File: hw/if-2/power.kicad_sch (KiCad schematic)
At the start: 21 parts, among them J5 Conn_01x02, U10 NCP1117-5.0_SOT223, U11 NCP1117-3.3_SOT223

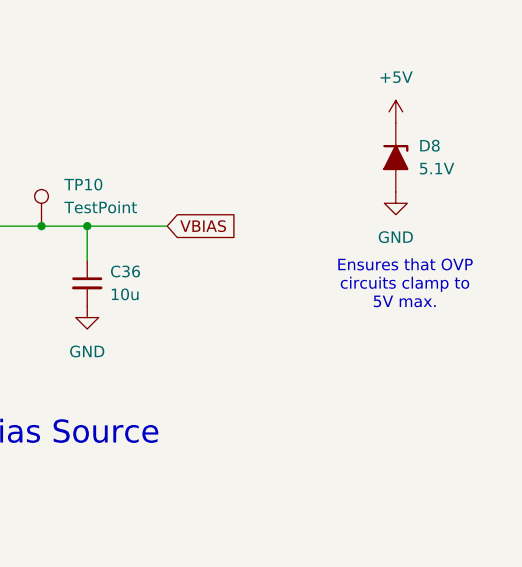
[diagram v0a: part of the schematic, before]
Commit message: Documentation improvements, moved a OVP circuit
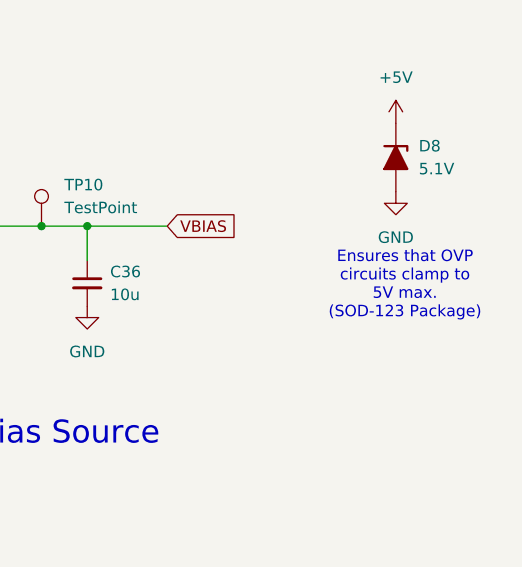
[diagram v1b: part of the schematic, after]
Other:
- note added: "Ensures that OVP circuits clamp to 5V max. (SOD-123 Package)"
- note removed: "Ensures that OVP circuits clamp to 5V max."
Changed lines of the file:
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@@
 	(title_block
 		(title "COS/CTCSS/PTT Controls (Radio 1)")
-		(date "2025-05-13")
+		(date "2025-05-31")
 		(rev "2")
 		(company "Bruce MacKinnon KC1FSZ")
@@
 		)
 	)
-	(text "Ensures that OVP \ncircuits clamp to \n5V max."
+	(text "Ensures that OVP \ncircuits clamp to \n5V max.\n(SOD-123 Package)"
 		(exclude_from_sim no)
 		(at 248.666 56.134 0)

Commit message: Updated audio file to 16K
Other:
- note added: "Band is on the cathode (this end)"
- note added: "Ensures that all OVP circuits clamp to 5V max. (SOD-123 Package)"
- note added: "Reverse polarity protection (marking "KL")"
- note removed: "Ensures that OVP circuits clamp to 5V max. (SOD-123 Package)"
- note removed: "Reverse polarity protection"
- title: COS/CTCSS/PTT Controls (Radio 1) -> Power
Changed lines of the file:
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@@
 	(paper "USLetter")
 	(title_block
-		(title "COS/CTCSS/PTT Controls (Radio 1)")
+		(title "Power")
 		(date "2025-06-21")
 		(rev "3")
@@
 		(comment 1 "Copyright (C) Bruce MacKinnon, 2025")
 		(comment 2 "NOT FOR COMMERCIAL USE")
+	)
+	(text "Band is on the \ncathode (this end)"
+		(exclude_from_sim no)
+		(at 237.744 37.846 0)
+		(effects
+			(font
+				(size 1.27 1.27)
+			)
+		)
 	)
 	(text "TVS Diode (12V_{wm}) for protection\nagainst ESD and other over-voltage transients."
@@
 		)
 	)
-	(text "Ensures that OVP \ncircuits clamp to \n5V max.\n(SOD-123 Package)"
+	(text "Ensures that all OVP \ncircuits clamp to \n5V max.\n(SOD-123 Package)"
 		(exclude_from_sim no)
 		(at 248.666 56.134 0)
@@
 		)
 	)
-	(text "Reverse polarity protection"
+	(text "Reverse polarity protection (marking \"KL\")"
 		(exclude_from_sim no)
 		(at 142.494 79.756 0)

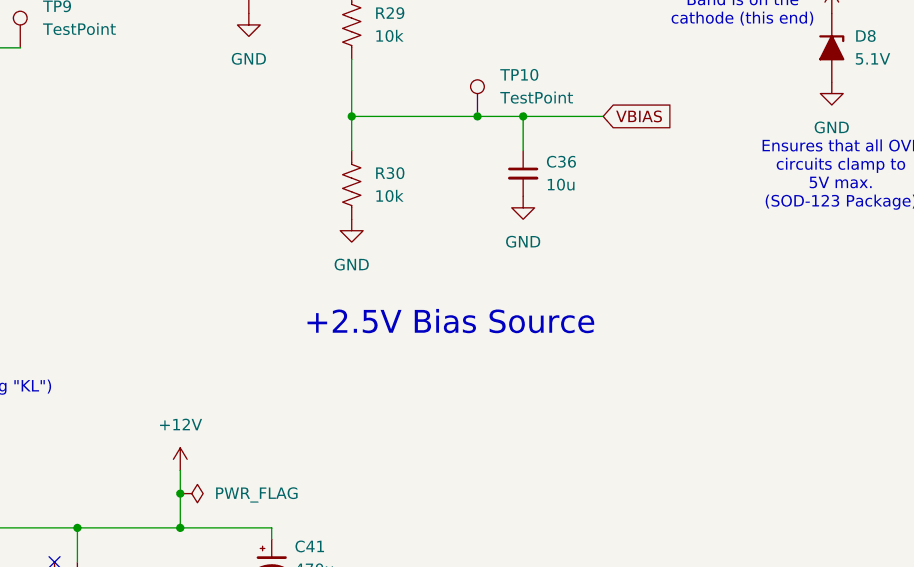
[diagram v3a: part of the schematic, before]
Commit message: Updating schematics, create new mini-board for radio interface
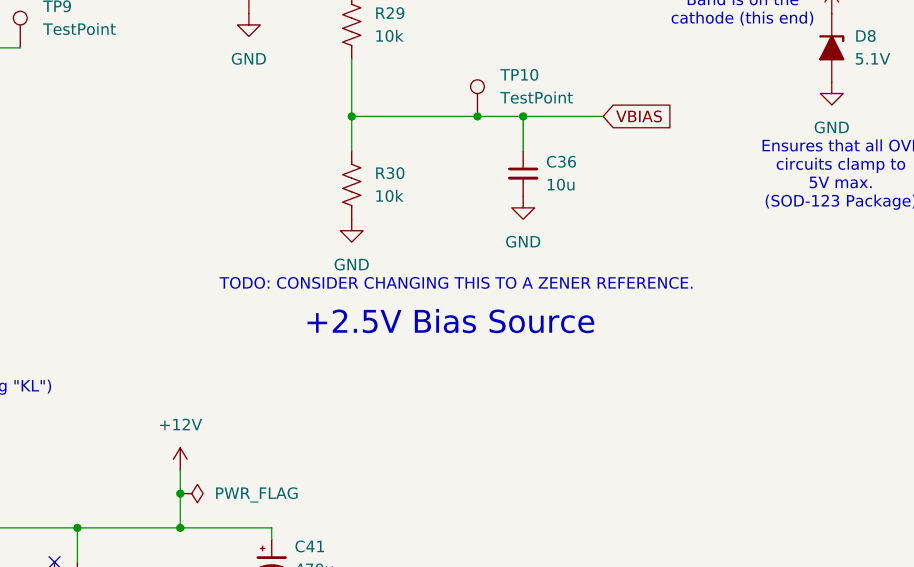
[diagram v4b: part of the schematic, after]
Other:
- note added: "TODO: CONSIDER CHANGING THIS TO A ZENER REFERENCE."
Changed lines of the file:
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@@
+		)
+	)
+	(text "TODO: CONSIDER CHANGING THIS TO A ZENER REFERENCE."
+		(exclude_from_sim no)
+		(at 205.994 68.326 0)
+		(effects
+			(font
+				(size 1.27 1.27)
+				(color 255 2 2 1)
+			)
 		)
 	)

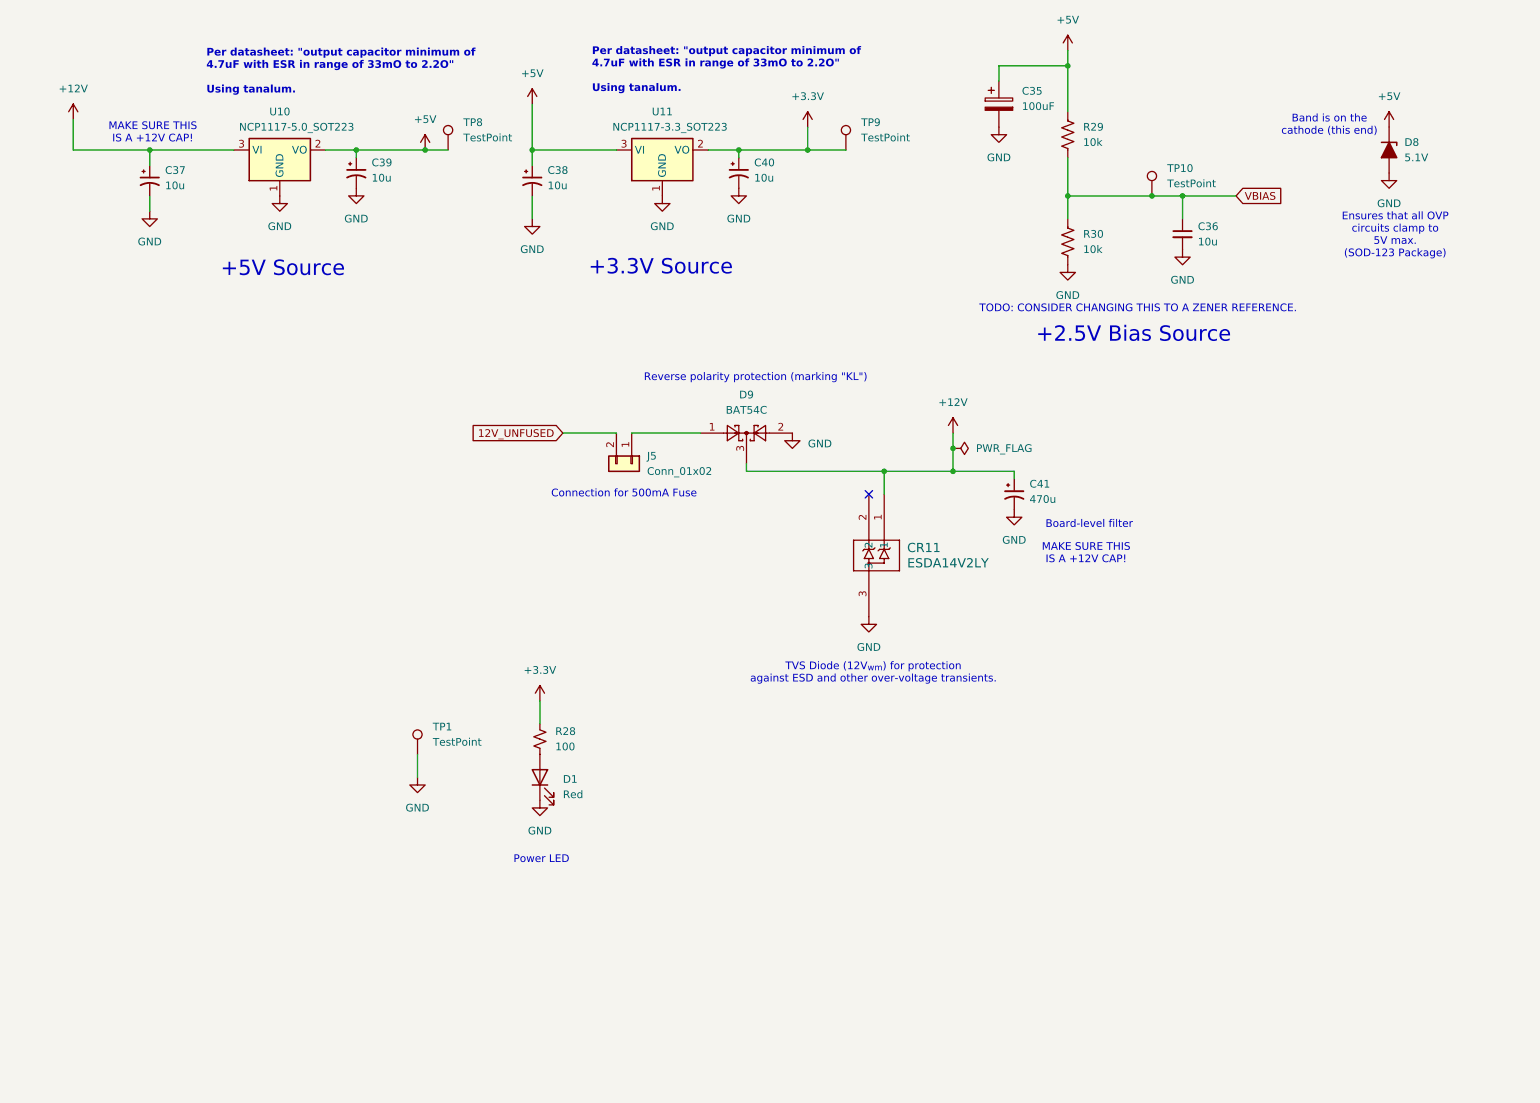
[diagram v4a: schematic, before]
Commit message: Updating schematics, create new mini-board for radio interface
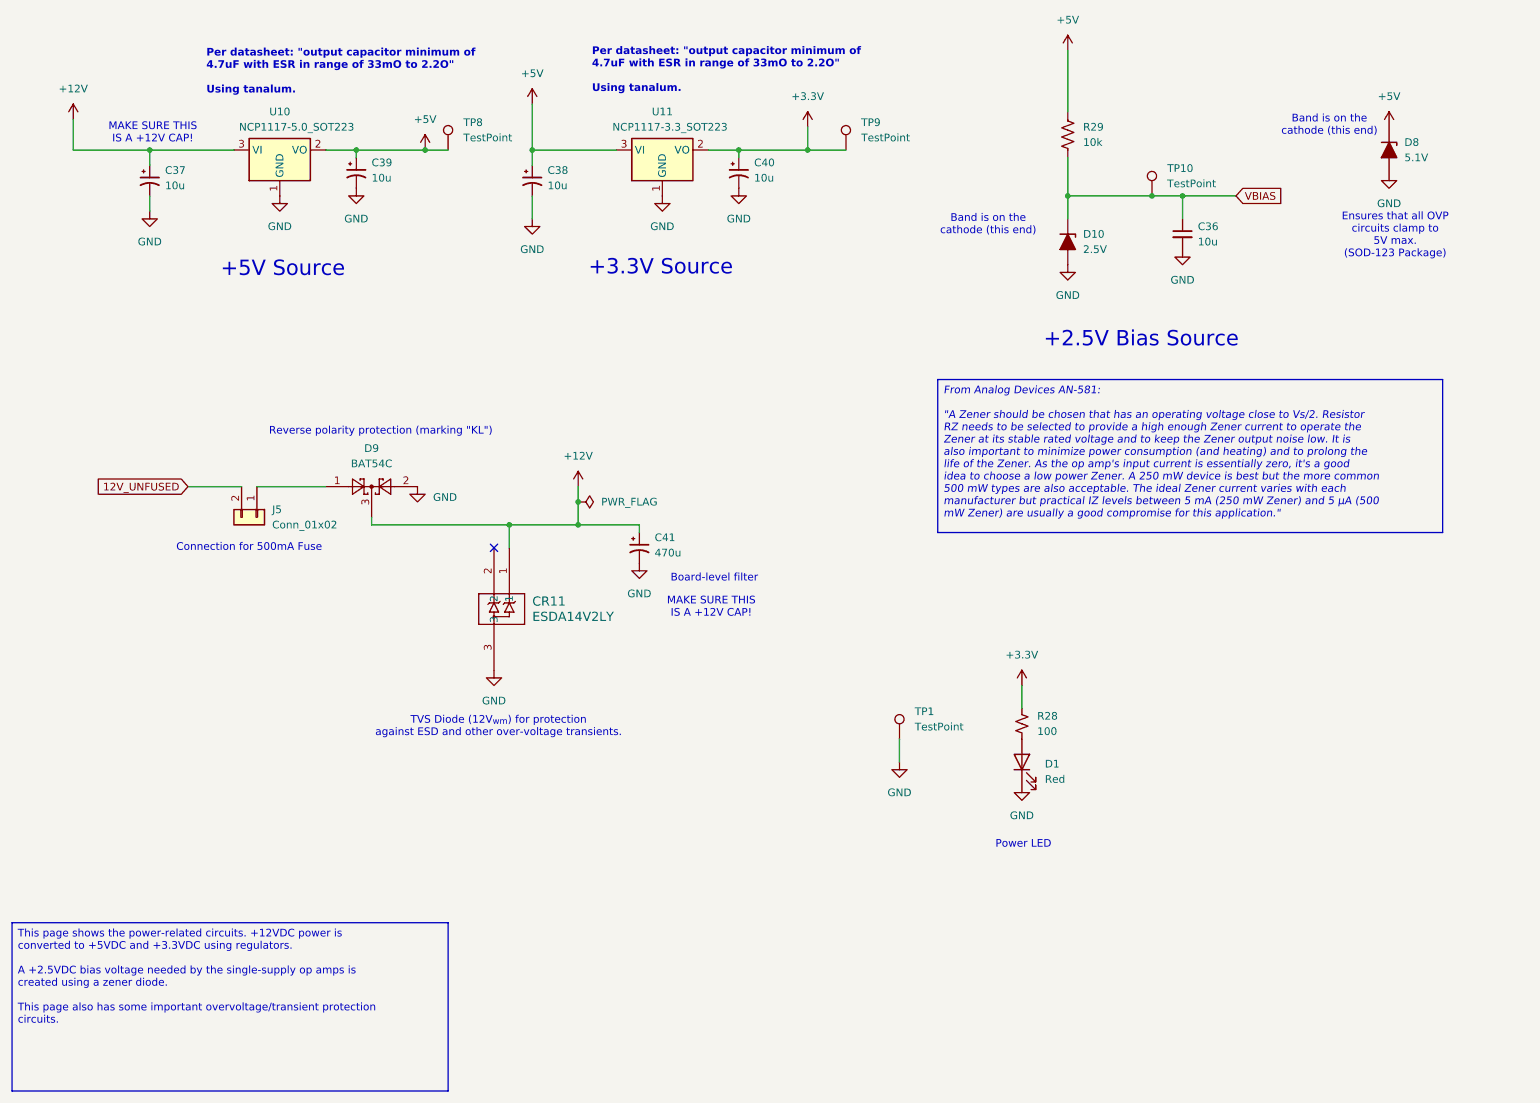
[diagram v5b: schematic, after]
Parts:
- removed C35: 100uF, Capacitor_THT:CP_Radial_D5.0mm_P2.50mm, symbol Device:C_Polarized
- removed R30: 10k, Resistor_SMD:R_0805_2012Metric_Pad1.20x1.40mm_HandSolder, symbol Device:R_US
- added D10: 2.5V, Diode_SMD:D_SOD-123, symbol Device:D_Zener_Filled
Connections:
- net GND: now also D10.2 (A)
- net VBIAS: now also D10.1 (K)
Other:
- note removed: "TODO: CONSIDER CHANGING THIS TO A ZENER REFERENCE."
- moved on the sheet: C41, CR11, D1, D9, J5, R28, TP1
